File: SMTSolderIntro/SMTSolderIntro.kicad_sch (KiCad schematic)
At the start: 138 parts, among them J1 USB_C_PWR_THRU, J2 Barrel_Jack, U1 NE556, U2 M74LCX04, U3 NE556

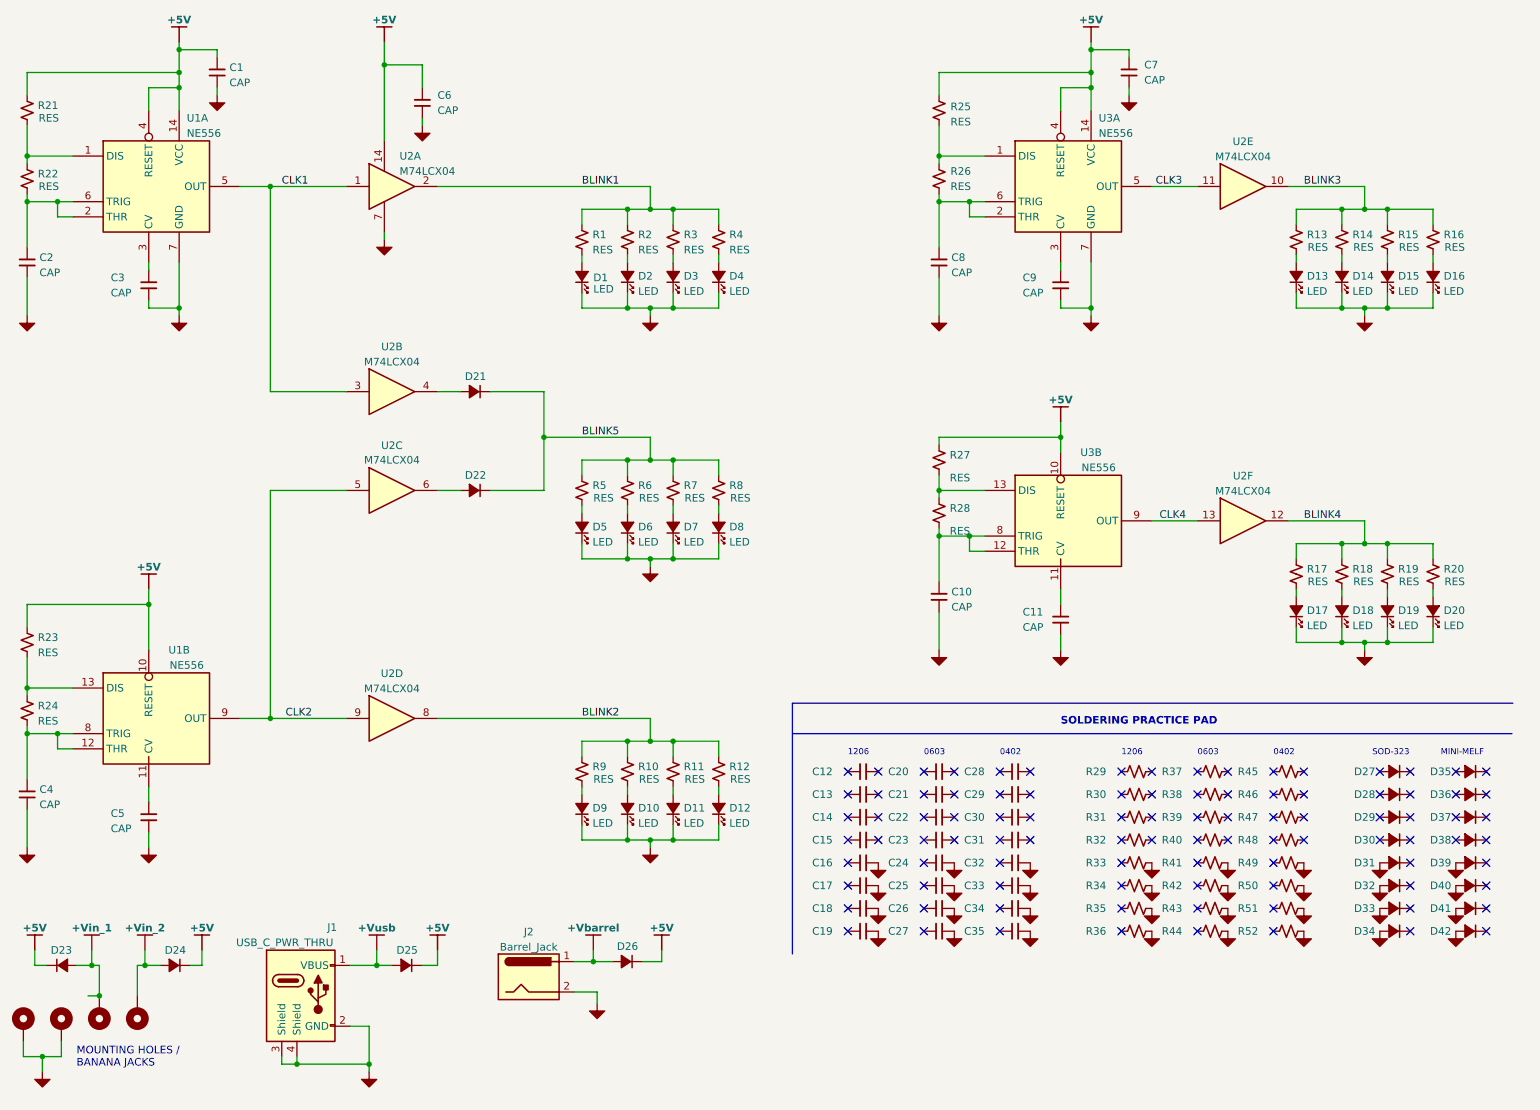
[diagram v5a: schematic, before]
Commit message: added some cap values, small sch changes for readability
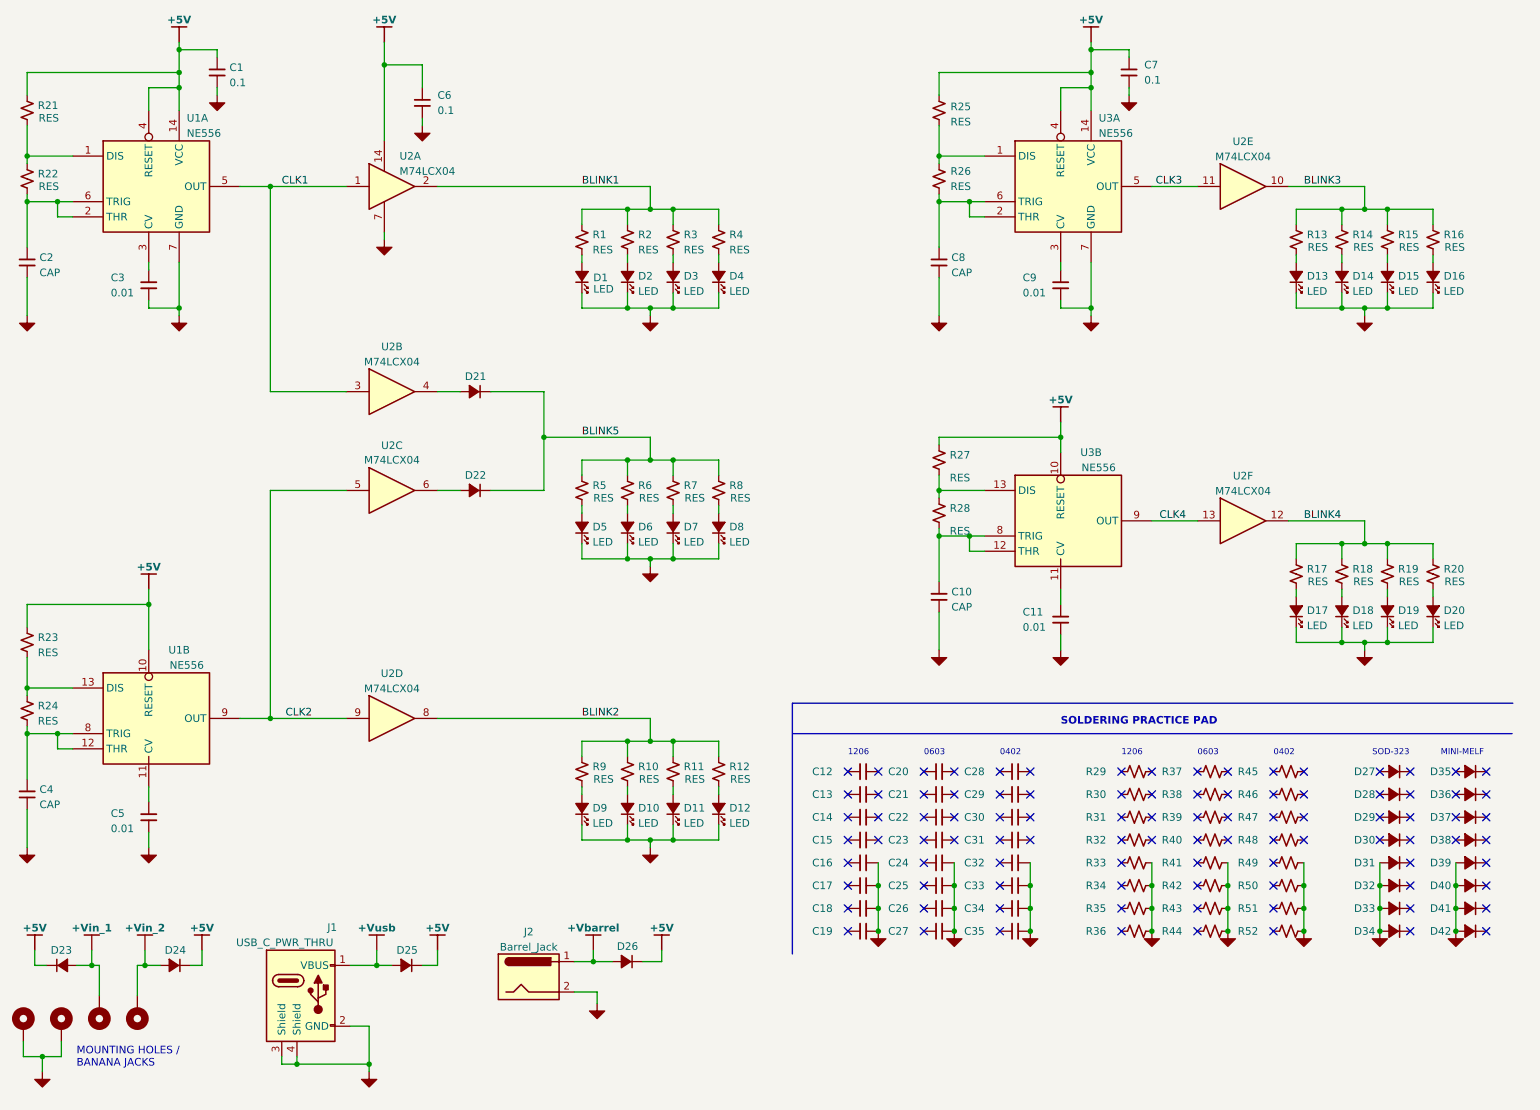
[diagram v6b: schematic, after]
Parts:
- C1, C6, C7: value CAP -> 0.1
- C11, C3, C5, C9: value CAP -> 0.01

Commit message: finalized 556 timer resistor and cap values for different flashing freqs, added some notes to the schematic, added flower images (will replace with better ones)
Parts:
- C10, C2, C4, C8: value CAP -> 0.01
- R21, R22, R23, R25: value RES -> 10M
- R24: value RES -> 8.2M
- R26, R27, R28: value RES -> 4.7M
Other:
- note added: "A kit for learning how to SMT solder"
- note added: "Blink rate: Flickering due to diode "or", mostly on."
- note added: "Blink rate: ~10 Hz"
- note added: "Blink rate: ~5 Hz"
- note added: "Blink rate: ~6 Hz"
- note added: "Blink rate: ~7.5 Hz"
- note added: "Blink rates are approximate and will vary from board to board due to variations in 5% resistor values."
- note added: "Customize your board by making the flowers whatever color you want (or multicolor!) Just match these resistor values with each color: RED, ORG, YEL, GRN: 1k BLUE: 470"
- note added: "HALF ARE GNDED FOR PRACTICE WITH HEAT SINKING PADS"
- title: (none) -> SMT Garden
- moved on the sheet: C10, C11, C7, C8, C9, R25, R26, R27, R28, U2E, U2F, U3A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
